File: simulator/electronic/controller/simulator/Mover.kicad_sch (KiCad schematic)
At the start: 4 parts, among them U2 STSPIN220

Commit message: design schematics
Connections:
- net PIN4 renamed SW_TOP
- net PIN5 renamed SW_CENTER
- net PIN6 renamed SW_BOTTOM
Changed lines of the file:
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@@
 		)
 	)
-	(hierarchical_label "PIN6"
+	(hierarchical_label "SW_BOTTOM"
 		(shape input)
 		(at 123.19 88.9 0)
@@
 		)
 	)
-	(hierarchical_label "PIN4"
+	(hierarchical_label "SW_TOP"
 		(shape input)
 		(at 123.19 83.82 0)
@@
 		)
 	)
-	(hierarchical_label "PIN5"
+	(hierarchical_label "SW_CENTER"
 		(shape input)
 		(at 123.19 86.36 0)
@@
 		(instances
 			(project "simulator"
+				(path "/84d97a1d-251a-442e-a359-d3f5e8dc9a44/0d78662d-4890-43f0-a9ec-125e8818156b"
+					(reference "CENTER3")
+					(unit 2)
+				)
+				(path "/84d97a1d-251a-442e-a359-d3f5e8dc9a44/59585693-1476-485c-a1f5-8452f6455381"
+					(reference "CENTER4")
+					(unit 2)
+				)
+				(path "/84d97a1d-251a-442e-a359-d3f5e8dc9a44/bd2ea943-255d-4c49-8333-92ca1fed74a4"
+					(reference "CENTER2")
+					(unit 2)
+				)
 				(path "/84d97a1d-251a-442e-a359-d3f5e8dc9a44/be2bbb03-78a3-442d-9154-7b2a25c4208e"
 					(reference "CENTER1")
@@
 		(instances
 			(project "simulator"
+				(path "/84d97a1d-251a-442e-a359-d3f5e8dc9a44/0d78662d-4890-43f0-a9ec-125e8818156b"
+					(reference "U4")
+					(unit 1)
+				)
+				(path "/84d97a1d-251a-442e-a359-d3f5e8dc9a44/59585693-1476-485c-a1f5-8452f6455381"
+					(reference "U5")
+					(unit 1)
+				)
+				(path "/84d97a1d-251a-442e-a359-d3f5e8dc9a44/bd2ea943-255d-4c49-8333-92ca1fed74a4"
+					(reference "U3")
+					(unit 1)
+				)
 				(path "/84d97a1d-251a-442e-a359-d3f5e8dc9a44/be2bbb03-78a3-442d-9154-7b2a25c4208e"
 					(reference "U2")
@@
 		(instances
 			(project "simulator"
+				(path "/84d97a1d-251a-442e-a359-d3f5e8dc9a44/0d78662d-4890-43f0-a9ec-125e8818156b"
+					(reference "#PWR09")
+					(unit 1)
+				)
+				(path "/84d97a1d-251a-442e-a359-d3f5e8dc9a44/59585693-1476-485c-a1f5-8452f6455381"
+					(reference "#PWR012")
+					(unit 1)
+				)
+				(path "/84d97a1d-251a-442e-a359-d3f5e8dc9a44/bd2ea943-255d-4c49-8333-92ca1fed74a4"
+					(reference "#PWR06")
+					(unit 1)
+				)
 				(path "/84d97a1d-251a-442e-a359-d3f5e8dc9a44/be2bbb03-78a3-442d-9154-7b2a25c4208e"
 					(reference "#PWR03")
@@
 		(instances
 			(project "simulator"
+				(path "/84d97a1d-251a-442e-a359-d3f5e8dc9a44/0d78662d-4890-43f0-a9ec-125e8818156b"
+					(reference "#PWR010")
+					(unit 1)
+				)
+				(path "/84d97a1d-251a-442e-a359-d3f5e8dc9a44/59585693-1476-485c-a1f5-8452f6455381"
+					(reference "#PWR013")
+					(unit 1)
+				)
+				(path "/84d97a1d-251a-442e-a359-d3f5e8dc9a44/bd2ea943-255d-4c49-8333-92ca1fed74a4"
+					(reference "#PWR07")
+					(unit 1)
+				)
 				(path "/84d97a1d-251a-442e-a359-d3f5e8dc9a44/be2bbb03-78a3-442d-9154-7b2a25c4208e"
 					(reference "#PWR02")
@@
 		(instances
 			(project "simulator"
+				(path "/84d97a1d-251a-442e-a359-d3f5e8dc9a44/0d78662d-4890-43f0-a9ec-125e8818156b"
+					(reference "TOP3")
+					(unit 1)
+				)
+				(path "/84d97a1d-251a-442e-a359-d3f5e8dc9a44/59585693-1476-485c-a1f5-8452f6455381"
+					(reference "TOP4")
+					(unit 1)
+				)
+				(path "/84d97a1d-251a-442e-a359-d3f5e8dc9a44/bd2ea943-255d-4c49-8333-92ca1fed74a4"
+					(reference "TOP2")
+					(unit 1)
+				)
 				(path "/84d97a1d-251a-442e-a359-d3f5e8dc9a44/be2bbb03-78a3-442d-9154-7b2a25c4208e"
 					(reference "TOP1")
@@
 		(instances
 			(project "simulator"
+				(path "/84d97a1d-251a-442e-a359-d3f5e8dc9a44/0d78662d-4890-43f0-a9ec-125e8818156b"
+					(reference "BOTTOM3")
+					(unit 2)
+				)
+				(path "/84d97a1d-251a-442e-a359-d3f5e8dc9a44/59585693-1476-485c-a1f5-8452f6455381"
+					(reference "BOTTOM4")
+					(unit 2)
+				)
+				(path "/84d97a1d-251a-442e-a359-d3f5e8dc9a44/bd2ea943-255d-4c49-8333-92ca1fed74a4"
+					(reference "BOTTOM2")
+					(unit 2)
+				)
 				(path "/84d97a1d-251a-442e-a359-d3f5e8dc9a44/be2bbb03-78a3-442d-9154-7b2a25c4208e"
 					(reference "BOTTOM1")

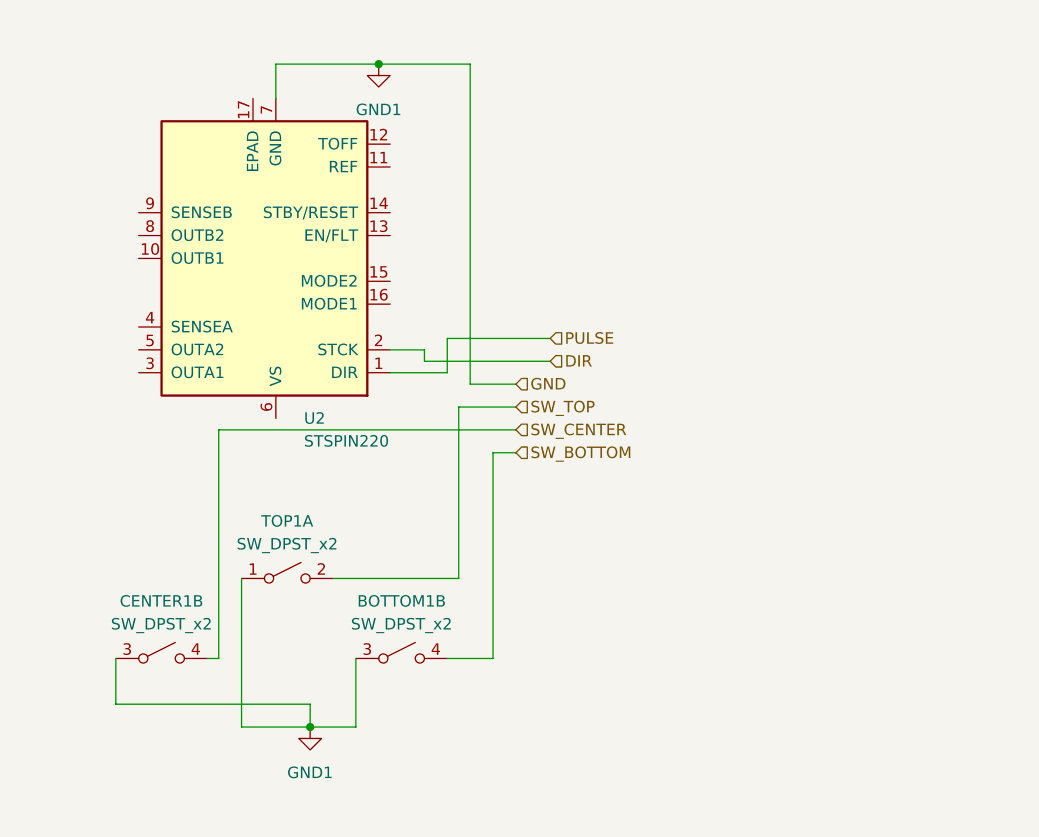
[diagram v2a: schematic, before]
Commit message: shaped schematic and PCB added printed documentation of PCB
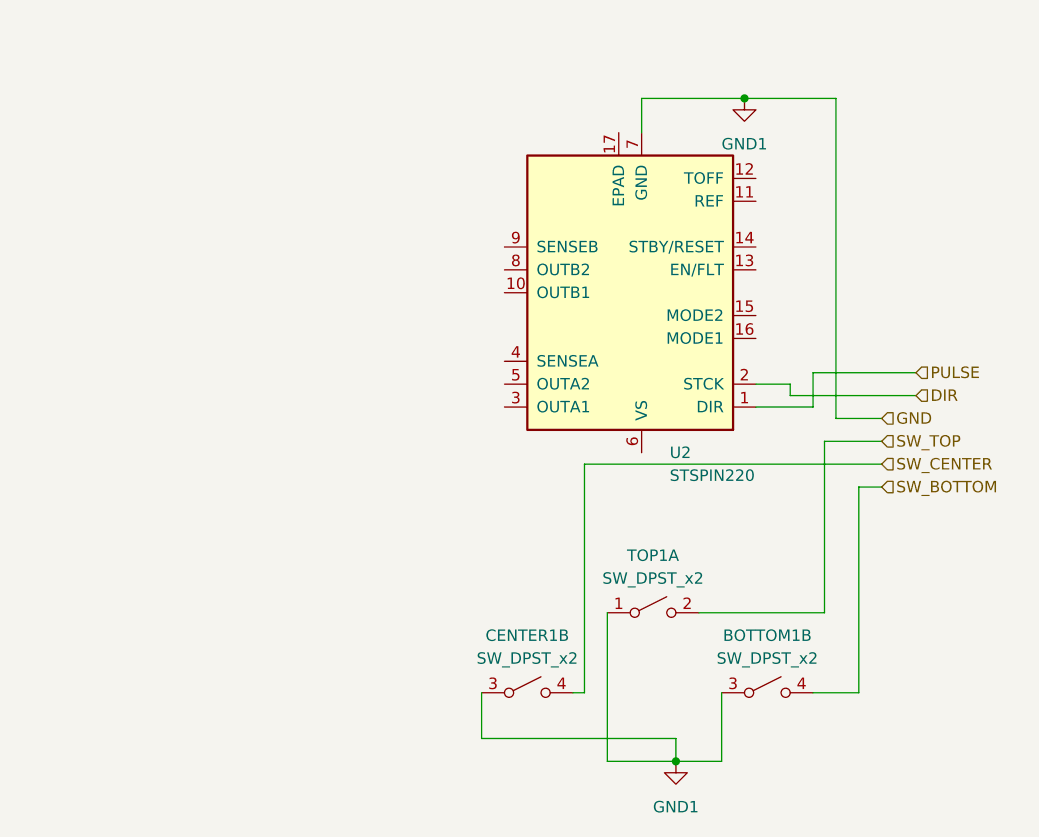
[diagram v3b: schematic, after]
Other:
- company: (none) -> HTL Leonding
- title: (none) -> Unseen-Obstacles - Simulator Controller
- moved on the sheet: BOTTOM1B, CENTER1B, TOP1A, U2

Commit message: finalized schematics and PCB
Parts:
- removed BOTTOM1, CENTER1, TOP1: SW_DPST_x2, symbol Switch:SW_DPST_x2
- removed U2: STSPIN220, Package_DFN_QFN:VQFN-16-1EP_3x3mm_P0.5mm_EP1.8x1.8mm, symbol Driver_Motor:STSPIN220
- added DSD1: DM542T, symbol UO_Electrical_Components:DM542T
- added M: Stepper (bipolar), symbol Motor:Stepper_Motor_bipolar
- added SW: TOP, symbol Switch:SW_Push_SPDT
- added SW2: CENTER, symbol Switch:SW_Push_SPDT
- added SW3: BOTTOM, symbol Switch:SW_Push_SPDT
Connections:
- net SW_BOTTOM: now also SW3.3 (C)
- net SW_CENTER: now also SW2.3 (C)
- net SW_TOP: now also SW.3 (C)
- new net: DSD1.12 (A-), M.1
- new net: DSD1.11 (A+), M.2 (-)
- new net: DSD1.13 (B+), M.3
- new net: DSD1.14 (B-), M.4
- new net GND_PWR: DSD1.9 (GND)
- new net SD_DIR: DSD1.3 (DIR+)
- new net SD_GND: DSD1.2 (PUL-), DSD1.4 (DIR-)
- new net SD_PULSE: DSD1.1 (PUL+)
- new net SW_COMMON: SW.2 (B), SW2.2 (B), SW3.2 (B)
- new net V_PWR: DSD1.10 (+Vdc)
- no-connect marks 0 -> 4

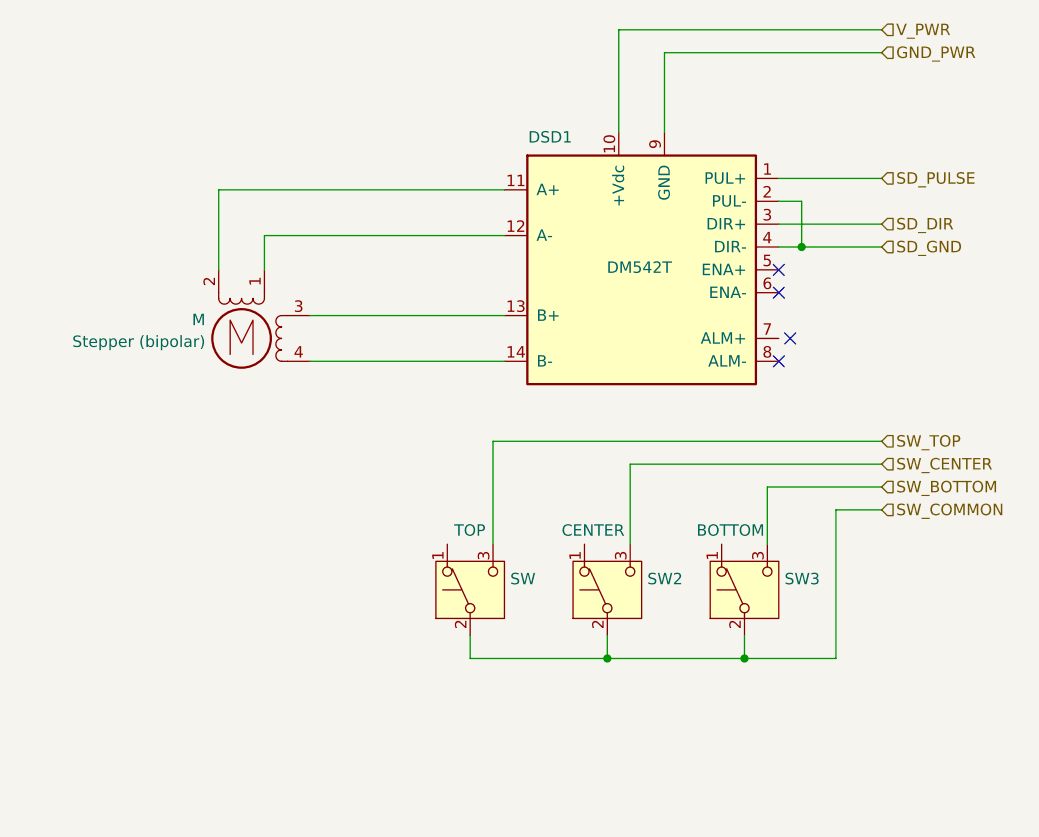
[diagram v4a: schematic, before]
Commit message: added stabilization Cos and alternative text
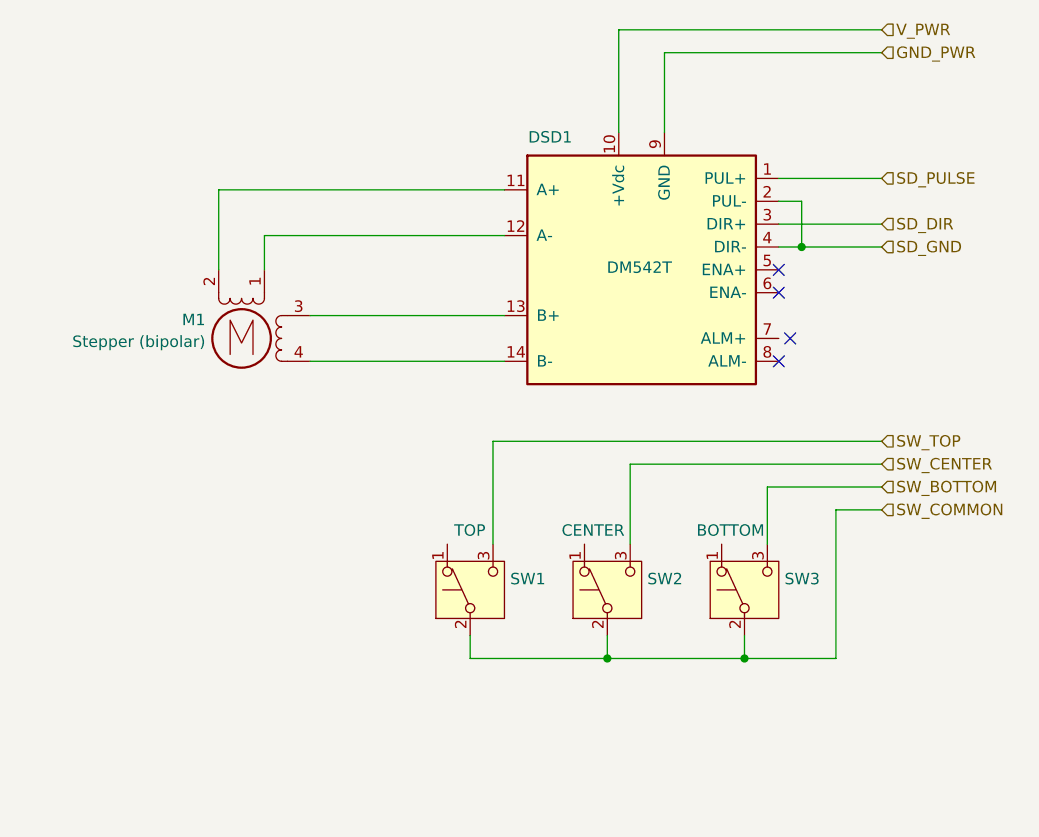
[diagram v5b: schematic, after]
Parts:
- renumbered M to M1, SW to SW1
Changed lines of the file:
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@@
 		(on_board yes)
 		(dnp no)
-		(property "Reference" "M"
+		(property "Reference" "M1"
 			(at 88.6968 74.1369 0)
 			(effects
@@
 				(path "/84d97a1d-251a-442e-a359-d3f5e8dc9a44/a0a784be-d584-478a-8147-f948bdeac8bb"
 					(reference "M3")
+					(unit 1)
+				)
+				(path "/84d97a1d-251a-442e-a359-d3f5e8dc9a44/be2bbb03-78a3-442d-9154-7b2a25c4208e"
+					(reference "M1")
 					(unit 1)
 				)
@@
 		(on_board yes)
 		(dnp no)
-		(property "Reference" "SW"
+		(property "Reference" "SW1"
 			(at 122.555 102.9278 90)
 			(effects
@@
 					(unit 1)
 				)
+				(path "/84d97a1d-251a-442e-a359-d3f5e8dc9a44/be2bbb03-78a3-442d-9154-7b2a25c4208e"
+					(reference "SW1")
+					(unit 1)
+				)
